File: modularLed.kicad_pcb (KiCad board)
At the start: 2 copper layers, 101.6 x 101.6 mm, 173 parts, among them IC101 ATMEGA328P-A, J101 POWER_JACKPTH, M301 FDS4935BZ, M302 FDS4935BZ, M303 FDS4935BZ, M304 FDS4935BZ, M305 FDS4935BZ, M306 FDS4935BZ, M307 FDS4935BZ, M308 FDS4935BZ, M401 FDS4935BZ, M402 FDS4935BZ, M403 FDS4935BZ, M404 FDS4935BZ, M405 FDS4935BZ, M406 FDS4935BZ, M407 FDS4935BZ, M408 FDS4935BZ, M501 FDS4935BZ, M502 FDS4935BZ, M503 FDS4935BZ, M504 FDS4935BZ, M505 FDS4935BZ, M506 FDS4935BZ, M507 FDS4935BZ, M508 FDS4935BZ, M601 FDS4935BZ, M602 FDS4935BZ, M603 FDS4935BZ, M604 FDS4935BZ, M605 FDS4935BZ, M606 FDS4935BZ, M607 FDS4935BZ, M608 FDS4935BZ, P101 CONN_01X04, P102 CONN_01X04, P103 CONN_01X04, P104 CONN_01X04, P105 CONN_01X06, P106 CONN_01X06, P107 CONN_01X06, P108 CONN_01X06, P109 CONN_02X03, P701 CONN_01X06, U101 ISL83485, U102 R-78E-0.5, U103 TLC5941, U104 74LS283, U105 74LS283, U201 74LS139, U301 74154, U401 74154, U501 74154, U601 74154, U701 ESP-12, U702 ISL83485

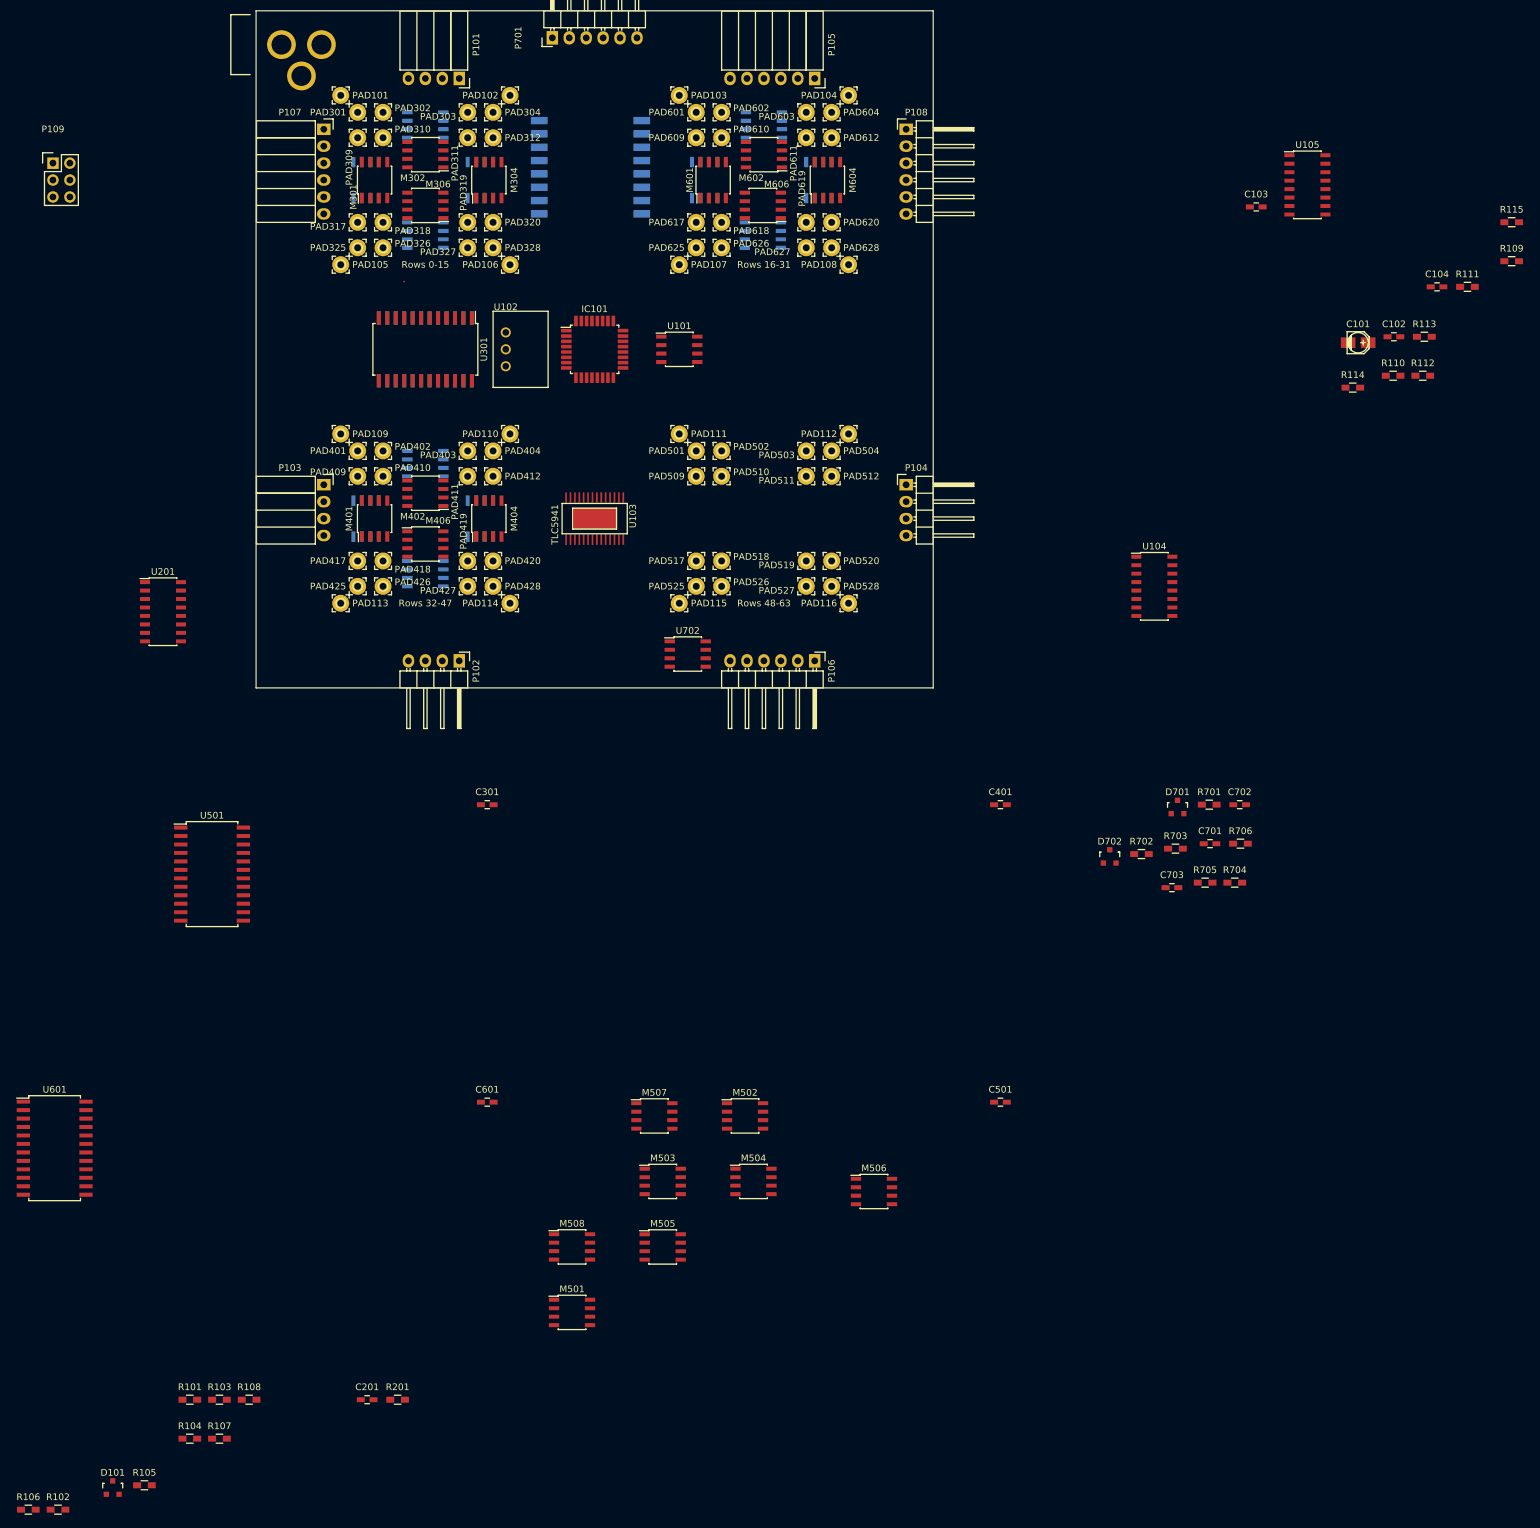
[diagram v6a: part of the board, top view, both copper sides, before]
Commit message: Rough component placement
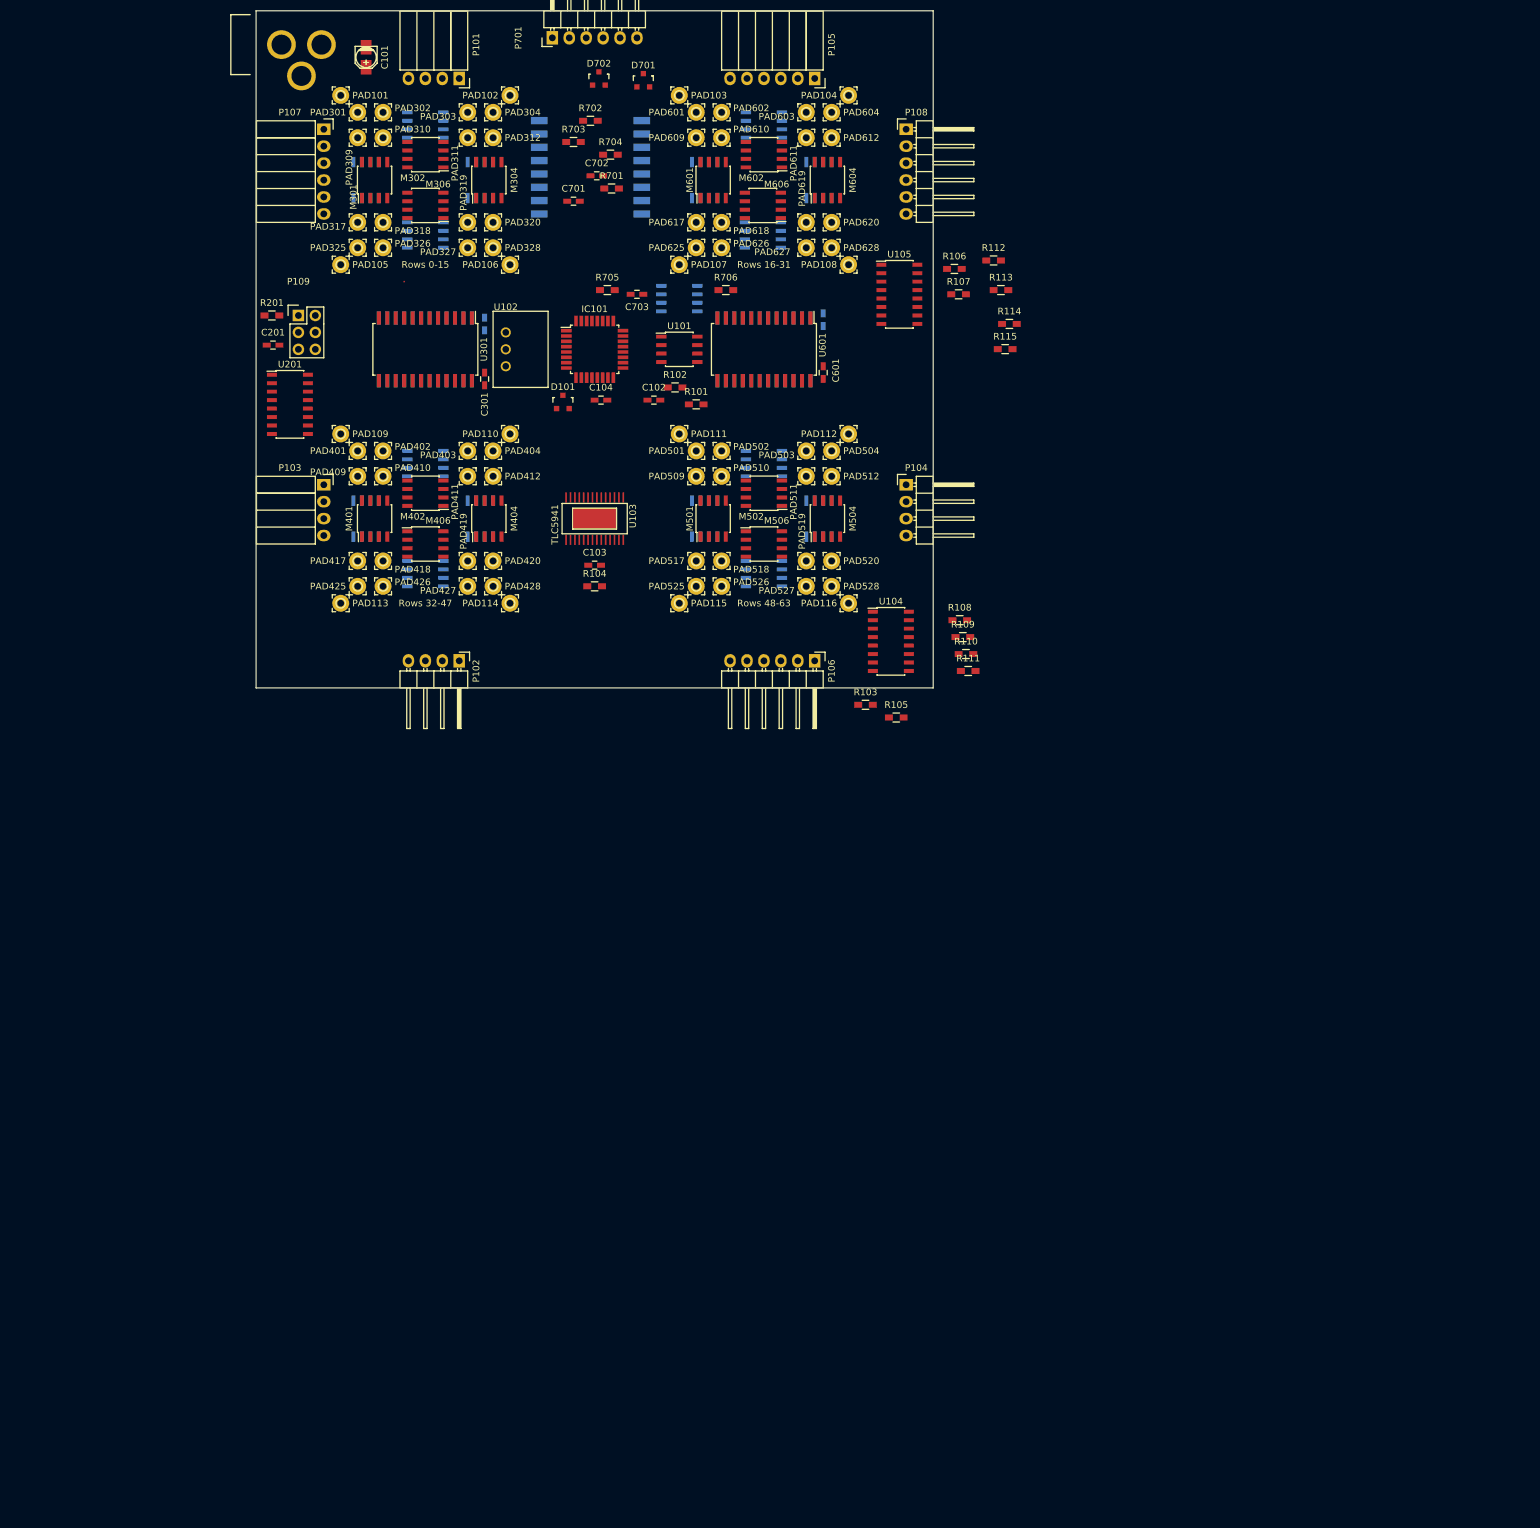
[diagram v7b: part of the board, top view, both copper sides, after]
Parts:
- C401, C501, M503, M505, M507, M508, U501, U702: moved to B.Cu
- moved R106 232.3 mm to (193.7, 89.5)
- moved R107 204.4 mm to (194.3, 93.3)
- moved R102 192.2 mm to (151.8, 107.3)
- moved D101 176.4 mm to (134.9, 109.5)
- moved R101 167.6 mm to (154.9, 109.9)
- moved R201 163.8 mm to (91.3, 96.5)
- moved R105 161.2 mm to (185.0, 156.8)
- moved U601 160.3 mm to (165.1, 101.6), turned to 270 degrees
- moved C201 158.9 mm to (91.4, 101.0)
- moved R108 158.3 mm to (194.5, 142.2)
- moved C101 154.9 mm to (105.4, 57.8), turned to 270 degrees
- moved R704 143.9 mm to (142.1, 72.4)
- moved R103 142.4 mm to (180.3, 154.9)
- moved R104 141.6 mm to (139.7, 137.2)
- moved D702 139.6 mm to (140.3, 61.0)
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
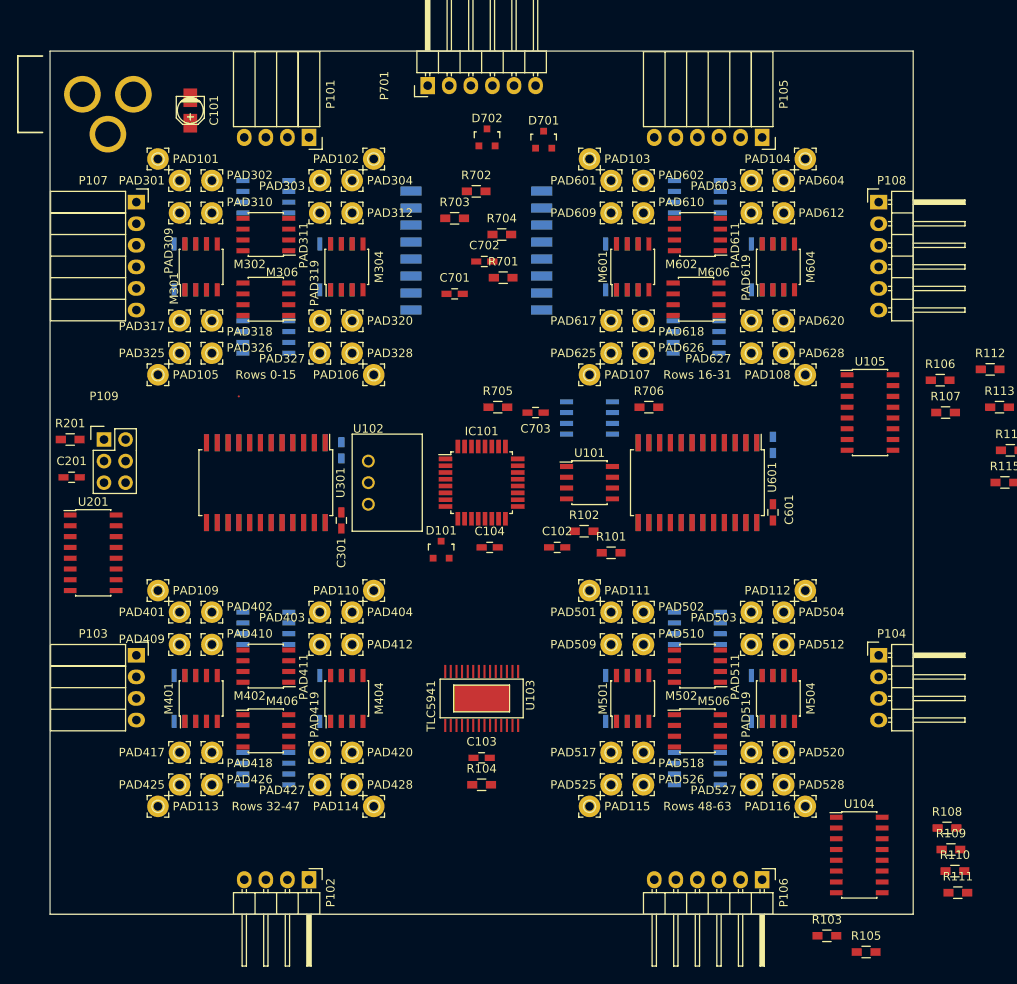
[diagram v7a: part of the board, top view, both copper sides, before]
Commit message: Improved connector placement
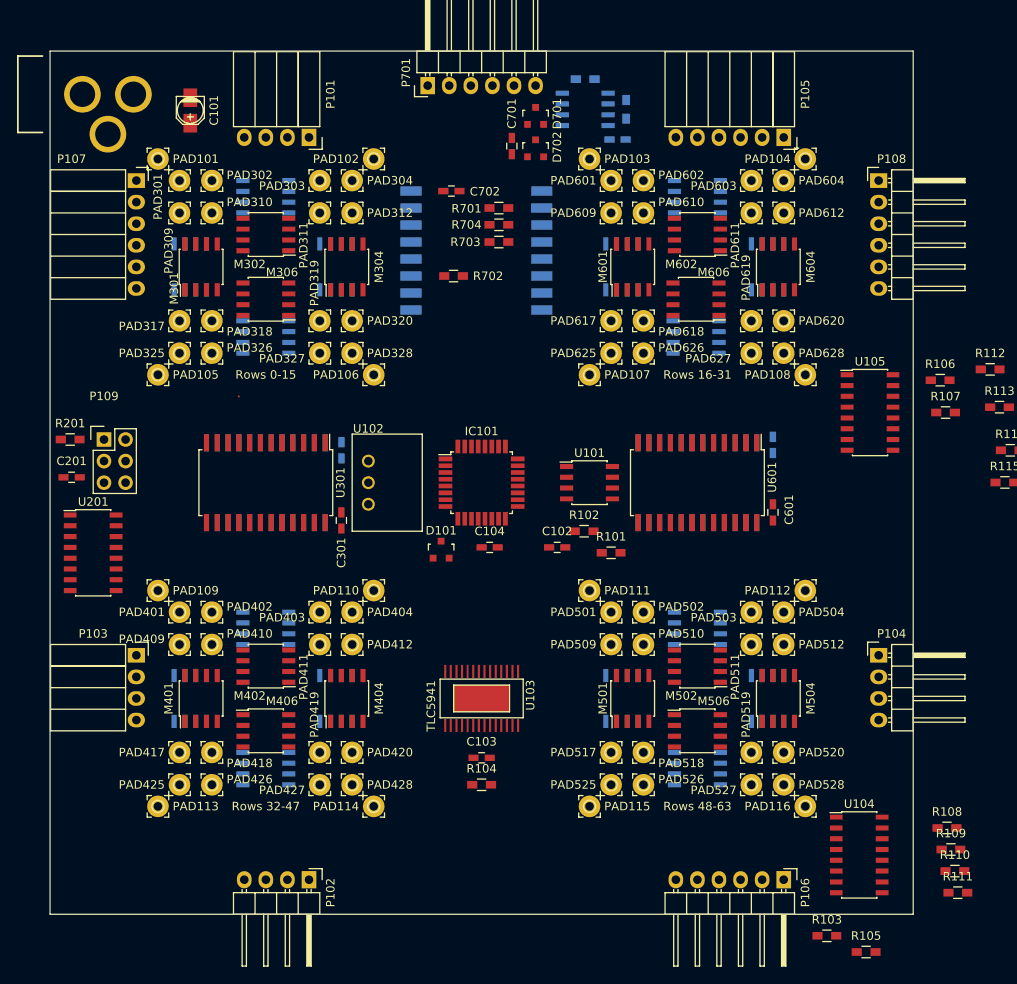
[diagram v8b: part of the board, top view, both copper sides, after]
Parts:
- C703, R705, R706: moved to B.Cu
- moved R705 40.0 mm to (151.9, 54.1), turned to 180 degrees
- moved U702 36.3 mm to (151.9, 57.7)
- moved R706 35.2 mm to (156.7, 57.7), turned to 90 degrees
- moved C703 33.5 mm to (155.7, 61.2)
- moved C701 18.7 mm to (143.3, 62.0), turned to 270 degrees
- moved R702 10.3 mm to (136.4, 77.3)
- moved C702 9.15 mm to (136.1, 67.3)
- moved R701 8.21 mm to (141.7, 69.3)
- moved R703 5.91 mm to (141.7, 73.3), turned to 180 degrees
- moved D702 5.85 mm to (146.1, 62.2)
- moved D701 2.97 mm to (146.1, 58.4)
- moved P105 2.54 mm to (175.3, 61.0)
- moved P106 2.54 mm to (175.3, 148.3)
- moved P107 2.54 mm to (99.1, 66.0)
- moved P108 2.54 mm to (186.4, 66.0)
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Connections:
- R706 pad 2: Net-(R706-Pad2) -> /RX+
